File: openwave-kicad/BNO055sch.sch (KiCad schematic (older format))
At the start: 1 part

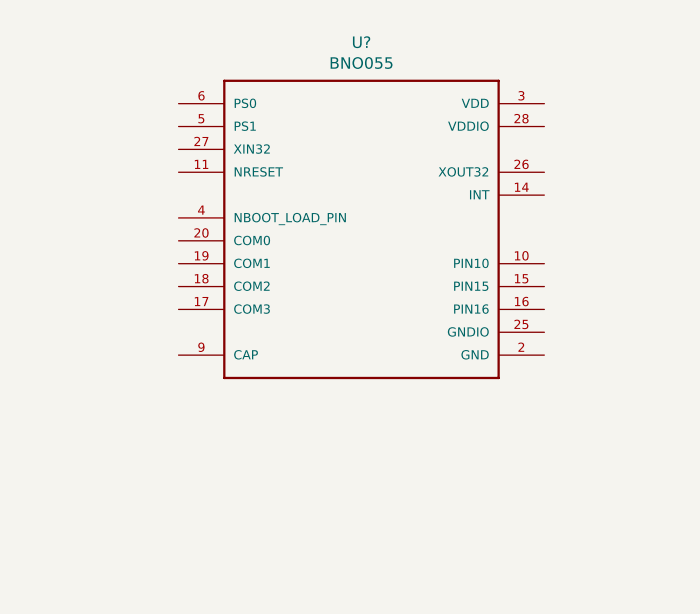
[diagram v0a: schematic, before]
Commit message: finished bno055 schematic
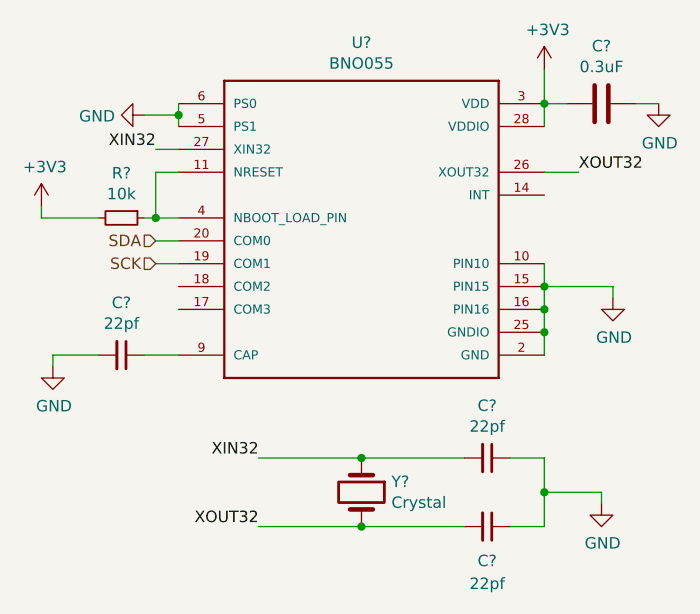
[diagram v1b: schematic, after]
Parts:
- added C?: 0.3uF, symbol Device:C
- added C? (x3): 22pf, symbol Device:C_Small
- added R?: 10k, symbol Device:R_Small
- added Y?: Crystal, symbol Device:Crystal
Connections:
- net GND: now reaches U?.10 (PIN10)
- net GND: now also U?.15 (PIN15), U?.16 (PIN16), U?.2 (GND), U?.25 (GNDIO), U?.5 (PS1), U?.6 (PS0), C?.1, C?.1, C?.1, C?.2
- net at U?.11 (NRESET): now also U?.4 (NBOOT_LOAD_PIN), R?.1
- net SCK: now reaches U?.19 (COM1)
- net SDA: now reaches U?.20 (COM0)
- net XOUT32: now reaches U?.26 (XOUT32)
- net XOUT32: now also C?.2, Y?.2
- net XIN32: now reaches U?.27 (XIN32)
- net XIN32: now also C?.2, Y?.1
- net +3V3: now reaches U?.28 (VDDIO)
- net +3V3: now also U?.3 (VDD), C?.2, R?.2
- net at U?.9 (CAP): now also C?.1
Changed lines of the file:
@@
 	1    0    0    -1
 $EndComp
+Wire Wire Line
+	6500 3950 6500 4050
+Connection ~ 6500 4050
+Wire Wire Line
+	6500 4050 6500 4150
+Wire Wire Line
+	6500 4050 6800 4050
+Wire Wire Line
+	6800 4050 6800 4100
+$Comp
+L power:GND #PWR?
+U 1 1 5CAA1777
+P 6800 4100
+F 0 "#PWR?" H 6800 3850 50  0001 C CNN
+F 1 "GND" H 6805 3927 50  0000 C CNN
+F 2 "" H 6800 4100 50  0001 C CNN
+F 3 "" H 6800 4100 50  0001 C CNN
+	1    6800 4100
+	1    0    0    -1
+$EndComp
+$Comp
+L power:GND #PWR?
+U 1 1 5CAA1805
+P 4750 3300
+F 0 "#PWR?" H 4750 3050 50  0001 C CNN
+F 1 "GND" V 4755 3172 50  0000 R CNN
+F 2 "" H 4750 3300 50  0001 C CNN
+F 3 "" H 4750 3300 50  0001 C CNN
+	1    4750 3300
+	0    1    1    0
+$EndComp
+Wire Wire Line
+	4900 3250 4900 3300
+Wire Wire Line
+	4750 3300 4900 3300
+Connection ~ 4900 3300
+Wire Wire Line
+	4900 3300 4900 3350
+Wire Wire Line
+	6500 3350 6500 3250
+Connection ~ 6500 3250
+$Comp
+L power:+3V3 #PWR?
+U 1 1 5CAA1959
+P 6500 3100
+F 0 "#PWR?" H 6500 2950 50  0001 C CNN
+F 1 "+3V3" H 6515 3273 50  0000 C CNN
+F 2 "" H 6500 3100 50  0001 C CNN
+F 3 "" H 6500 3100 50  0001 C CNN
+	1    6500 3100
+	1    0    0    -1
+$EndComp
+$Comp
+L Device:C C?
+U 1 1 5CAA1993
+P 6750 3250
+F 0 "C?" V 6498 3250 50  0000 C CNN
+F 1 "0.3uF" V 6589 3250 50  0000 C CNN
+F 2 "" H 6788 3100 50  0001 C CNN
+F 3 "~" H 6750 3250 50  0001 C CNN
+	1    6750 3250
+	0    1    1    0
+$EndComp
+$Comp
+L power:GND #PWR?
+U 1 1 5CAA1A96
+P 7000 3250
+F 0 "#PWR?" H 7000 3000 50  0001 C CNN
+F 1 "GND" H 7005 3077 50  0000 C CNN
+F 2 "" H 7000 3250 50  0001 C CNN
+F 3 "" H 7000 3250 50  0001 C CNN
+	1    7000 3250
+	1    0    0    -1
+$EndComp
+Wire Wire Line
+	6500 3100 6500 3250
+Wire Wire Line
+	6500 3250 6600 3250
+Wire Wire Line
+	6900 3250 7000 3250
+Text Label 4800 3450 2    50   ~ 0
+XIN32
+Wire Wire Line
+	4800 3450 4900 3450
+Text Label 6650 3550 0    50   ~ 0
+XOUT32
+Wire Wire Line
+	6500 3550 6650 3550
+$Comp
+L Device:Crystal Y?
+U 1 1 5CAA1D9E
+P 5700 4950
+F 0 "Y?" V 5654 5081 50  0000 L CNN
+F 1 "Crystal" V 5745 5081 50  0000 L CNN
+F 2 "" H 5700 4950 50  0001 C CNN
+F 3 "~" H 5700 4950 50  0001 C CNN
+	1    5700 4950
+	0    1    1    0
+$EndComp
+Text Label 5250 4800 2    50   ~ 0
+XIN32
+Text Label 5250 5100 2    50   ~ 0
+XOUT32
+Wire Wire Line
+	5250 4800 5700 4800
+Wire Wire Line
+	5250 5100 5700 5100
+$Comp
+L Device:C_Small C?
+U 1 1 5CAA202E
+P 6250 4800
+F 0 "C?" V 6021 4800 50  0000 C CNN
+F 1 "22pf" V 6112 4800 50  0000 C CNN
+F 2 "" H 6250 4800 50  0001 C CNN
+F 3 "~" H 6250 4800 50  0001 C CNN
+	1    6250 4800
+	0    1    1    0
+$EndComp
+$Comp
+L Device:C_Small C?
+U 1 1 5CAA2127
+P 6250 5100
+F 0 "C?" V 6400 5100 50  0000 C CNN
+F 1 "22pf" V 6500 5100 50  0000 C CNN
+F 2 "" H 6250 5100 50  0001 C CNN
+F 3 "~" H 6250 5100 50  0001 C CNN
+	1    6250 5100
+	0    1    1    0
+$EndComp
+Wire Wire Line
+	5700 5100 6150 5100
+Connection ~ 5700 5100
+Wire Wire Line
+	5700 4800 6150 4800
+Connection ~ 5700 4800
+Wire Wire Line
+	6350 4800 6500 4800
+Wire Wire Line
+	6500 4800 6500 4950
+Wire Wire Line
+	6500 5100 6350 5100
+Wire Wire Line
+	6500 4950 6750 4950
+Wire Wire Line
+	6750 4950 6750 5000
+Connection ~ 6500 4950
+Wire Wire Line
+	6500 4950 6500 5100
+$Comp
+L power:GND #PWR?
+U 1 1 5CAA276D
+P 6750 5000
+F 0 "#PWR?" H 6750 4750 50  0001 C CNN
+F 1 "GND" H 6755 4827 50  0000 C CNN
+F 2 "" H 6750 5000 50  0001 C CNN
+F 3 "" H 6750 5000 50  0001 C CNN
+	1    6750 5000
+	1    0    0    -1
+$EndComp
+$Comp
+L Device:C_Small C?
+U 1 1 5CAA289A
+P 4650 4350
+F 0 "C?" V 4421 4350 50  0000 C CNN
+F 1 "22pf" V 4512 4350 50  0000 C CNN
+F 2 "" H 4650 4350 50  0001 C CNN
+F 3 "~" H 4650 4350 50  0001 C CNN
+	1    4650 4350
+	0    1    1    0
+$EndComp
+$Comp
+L power:GND #PWR?
+U 1 1 5CAA293A
+P 4350 4400
+F 0 "#PWR?" H 4350 4150 50  0001 C CNN
+F 1 "GND" H 4355 4227 50  0000 C CNN
+F 2 "" H 4350 4400 50  0001 C CNN
+F 3 "" H 4350 4400 50  0001 C CNN
+	1    4350 4400
+	1    0    0    -1
+$EndComp
+Wire Wire Line
+	4350 4400 4350 4350
+Wire Wire Line
+	4350 4350 4550 4350
+Wire Wire Line
+	4750 4350 4900 4350
+Wire Wire Line
+	6500 4350 6500 4250
+Wire Wire Line
+	6500 4250 6500 4150
+Connection ~ 6500 4250
+Connection ~ 6500 4150
+$Comp
+L Device:R_Small R?
+U 1 1 5CAA3754
+P 4650 3750
+F 0 "R?" V 4454 3750 50  0000 C CNN
+F 1 "10k" V 4545 3750 50  0000 C CNN
+F 2 "" H 4650 3750 50  0001 C CNN
+F 3 "~" H 4650 3750 50  0001 C CNN
+	1    4650 3750
+	0    1    1    0
+$EndComp
+$Comp
+L power:+3V3 #PWR?
+U 1 1 5CAA3896
+P 4300 3700
+F 0 "#PWR?" H 4300 3550 50  0001 C CNN
+F 1 "+3V3" H 4315 3873 50  0000 C CNN
+F 2 "" H 4300 3700 50  0001 C CNN
+F 3 "" H 4300 3700 50  0001 C CNN
+	1    4300 3700
+	1    0    0    -1
+$EndComp
+Wire Wire Line
+	4300 3700 4300 3750
+Wire Wire Line
+	4300 3750 4550 3750
+Wire Wire Line
+	4750 3750 4800 3750
+Wire Wire Line
+	4900 3550 4800 3550
+Wire Wire Line
+	4800 3550 4800 3750
+Connection ~ 4800 3750
+Wire Wire Line
+	4800 3750 4900 3750
+Text HLabel 4800 3850 0    50   Input ~ 0
+SDA
+Wire Wire Line
+	4800 3850 4900 3850
+Text HLabel 4800 3950 0    50   Input ~ 0
+SCK
+Wire Wire Line
+	4800 3950 4900 3950
 $EndSCHEMATC

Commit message: linked all footprints to symbols, ready for routing
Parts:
- removed C?: 0.3uF, symbol Device:C
- C19: renamed from C?; footprint (none) -> Capacitor_SMD:C_0603_1608Metric
- C20, C21: renamed from C?; value 22pf -> 12pf; footprint (none) -> Capacitor_SMD:C_0603_1608Metric
- R12: renamed from R?; footprint (none) -> Resistor_SMD:R_0603_1608Metric
- U3: renamed from U?; footprint LGA28R50P4X10_380X520X100 -> BNO055:LGA28R50P4X10_380X520X100
- Y3: renamed from Y?; footprint (none) -> my_footprints:ABS06-32.768KHZ_smd_crystal
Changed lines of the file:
@@
 $EndDescr
 $Comp
-L wattnotions:BNO055 U?
+L wattnotions:BNO055 U3
 U 1 1 5CAEDCF4
 P 5700 3750
-F 0 "U?" H 5700 4517 50  0000 C CNN
+F 0 "U3" H 5700 4517 50  0000 C CNN
 F 1 "BNO055" H 5700 4426 50  0000 C CNN
-F 2 "LGA28R50P4X10_380X520X100" H 5700 3750 50  0001 L BNN
+F 2 "BNO055:LGA28R50P4X10_380X520X100" H 5700 3750 50  0001 L BNN
 F 3 "None" H 5700 3750 50  0001 L BNN
 F 4 "BNO055" H 5700 3750 50  0001 L BNN "Field4"
@@
 	6800 4050 6800 4100
 $Comp
-L power:GND #PWR?
+L power:GND #PWR0114
 U 1 1 5CAA1777
 P 6800 4100
-F 0 "#PWR?" H 6800 3850 50  0001 C CNN
+F 0 "#PWR0114" H 6800 3850 50  0001 C CNN
 F 1 "GND" H 6805 3927 50  0000 C CNN
 F 2 "" H 6800 4100 50  0001 C CNN
@@
 $EndComp
 $Comp
-L power:GND #PWR?
+L power:GND #PWR0115
 U 1 1 5CAA1805
 P 4750 3300
-F 0 "#PWR?" H 4750 3050 50  0001 C CNN
+F 0 "#PWR0115" H 4750 3050 50  0001 C CNN
 F 1 "GND" V 4755 3172 50  0000 R CNN
 F 2 "" H 4750 3300 50  0001 C CNN
@@
 Connection ~ 6500 3250
 $Comp
-L power:+3V3 #PWR?
+L power:+3V3 #PWR0116
 U 1 1 5CAA1959
 P 6500 3100
-F 0 "#PWR?" H 6500 2950 50  0001 C CNN
+F 0 "#PWR0116" H 6500 2950 50  0001 C CNN
 F 1 "+3V3" H 6515 3273 50  0000 C CNN
 F 2 "" H 6500 3100 50  0001 C CNN
@@
 	1    0    0    -1
 $EndComp
-$Comp
-L Device:C C?
-U 1 1 5CAA1993
-P 6750 3250
-F 0 "C?" V 6498 3250 50  0000 C CNN
-F 1 "0.3uF" V 6589 3250 50  0000 C CNN
-F 2 "" H 6788 3100 50  0001 C CNN
-F 3 "~" H 6750 3250 50  0001 C CNN
-	1    6750 3250
-	0    1    1    0
-$EndComp
-$Comp
-L power:GND #PWR?
-U 1 1 5CAA1A96
-P 7000 3250
-F 0 "#PWR?" H 7000 3000 50  0001 C CNN
-F 1 "GND" H 7005 3077 50  0000 C CNN
-F 2 "" H 7000 3250 50  0001 C CNN
-F 3 "" H 7000 3250 50  0001 C CNN
-	1    7000 3250
-	1    0    0    -1
-$EndComp
 Wire Wire Line
 	6500 3100 6500 3250
-Wire Wire Line
-	6500 3250 6600 3250
-Wire Wire Line
-	6900 3250 7000 3250
 Text Label 4800 3450 2    50   ~ 0
 XIN32
@@
 	6500 3550 6650 3550
 $Comp
-L Device:Crystal Y?
+L Device:Crystal Y3
 U 1 1 5CAA1D9E
 P 5700 4950
-F 0 "Y?" V 5654 5081 50  0000 L CNN
+F 0 "Y3" V 5654 5081 50  0000 L CNN
 F 1 "Crystal" V 5745 5081 50  0000 L CNN
-F 2 "" H 5700 4950 50  0001 C CNN
+F 2 "my_footprints:ABS06-32.768KHZ_smd_crystal" H 5700 4950 50  0001 C CNN
 F 3 "~" H 5700 4950 50  0001 C CNN
 	1    5700 4950
@@
 	5250 5100 5700 5100
 $Comp
-L Device:C_Small C?
+L Device:C_Small C20
 U 1 1 5CAA202E
 P 6250 4800
-F 0 "C?" V 6021 4800 50  0000 C CNN
-F 1 "22pf" V 6112 4800 50  0000 C CNN
-F 2 "" H 6250 4800 50  0001 C CNN
+F 0 "C20" V 6021 4800 50  0000 C CNN
+F 1 "12pf" V 6112 4800 50  0000 C CNN
+F 2 "Capacitor_SMD:C_0603_1608Metric" H 6250 4800 50  0001 C CNN
 F 3 "~" H 6250 4800 50  0001 C CNN
 	1    6250 4800
@@
 $EndComp
 $Comp
-L Device:C_Small C?
+L Device:C_Small C21
 U 1 1 5CAA2127
 P 6250 5100
-F 0 "C?" V 6400 5100 50  0000 C CNN
-F 1 "22pf" V 6500 5100 50  0000 C CNN
-F 2 "" H 6250 5100 50  0001 C CNN
+F 0 "C21" V 6400 5100 50  0000 C CNN
+F 1 "12pf" V 6500 5100 50  0000 C CNN
+F 2 "Capacitor_SMD:C_0603_1608Metric" H 6250 5100 50  0001 C CNN
 F 3 "~" H 6250 5100 50  0001 C CNN
 	1    6250 5100
@@
 	6500 4950 6500 5100
 $Comp
-L power:GND #PWR?
+L power:GND #PWR0118
 U 1 1 5CAA276D
 P 6750 5000
-F 0 "#PWR?" H 6750 4750 50  0001 C CNN
+F 0 "#PWR0118" H 6750 4750 50  0001 C CNN
 F 1 "GND" H 6755 4827 50  0000 C CNN
 F 2 "" H 6750 5000 50  0001 C CNN
@@
 $EndComp
 $Comp
-L Device:C_Small C?
+L Device:C_Small C19
 U 1 1 5CAA289A
 P 4650 4350
-F 0 "C?" V 4421 4350 50  0000 C CNN
+F 0 "C19" V 4421 4350 50  0000 C CNN
 F 1 "22pf" V 4512 4350 50  0000 C CNN
-F 2 "" H 4650 4350 50  0001 C CNN
+F 2 "Capacitor_SMD:C_0603_1608Metric" H 4650 4350 50  0001 C CNN
 F 3 "~" H 4650 4350 50  0001 C CNN
 	1    4650 4350
@@
 $EndComp
 $Comp
-L power:GND #PWR?
+L power:GND #PWR0119
 U 1 1 5CAA293A
 P 4350 4400
-F 0 "#PWR?" H 4350 4150 50  0001 C CNN
+F 0 "#PWR0119" H 4350 4150 50  0001 C CNN
 F 1 "GND" H 4355 4227 50  0000 C CNN
 F 2 "" H 4350 4400 50  0001 C CNN
@@
 Connection ~ 6500 4150
 $Comp
-L Device:R_Small R?
+L Device:R_Small R12
 U 1 1 5CAA3754
 P 4650 3750
-F 0 "R?" V 4454 3750 50  0000 C CNN
+F 0 "R12" V 4454 3750 50  0000 C CNN
 F 1 "10k" V 4545 3750 50  0000 C CNN
-F 2 "" H 4650 3750 50  0001 C CNN
+F 2 "Resistor_SMD:R_0603_1608Metric" H 4650 3750 50  0001 C CNN
 F 3 "~" H 4650 3750 50  0001 C CNN
 	1    4650 3750
@@
 $EndComp
 $Comp
-L power:+3V3 #PWR?
+L power:+3V3 #PWR0120
 U 1 1 5CAA3896
 P 4300 3700
-F 0 "#PWR?" H 4300 3550 50  0001 C CNN
+F 0 "#PWR0120" H 4300 3550 50  0001 C CNN
 F 1 "+3V3" H 4315 3873 50  0000 C CNN
 F 2 "" H 4300 3700 50  0001 C CNN
